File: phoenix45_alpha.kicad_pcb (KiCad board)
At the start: 2 copper layers, 247.7 x 77.5 mm, 125 parts, among them J1 AVR-ISP-6, SW1 SW_PUSH, SW2 SW_PUSH, U1 SRV05-4, U2 ATmega32U4-M, U3 ATmega32U4-M, X1 Crystal_GND24_Small

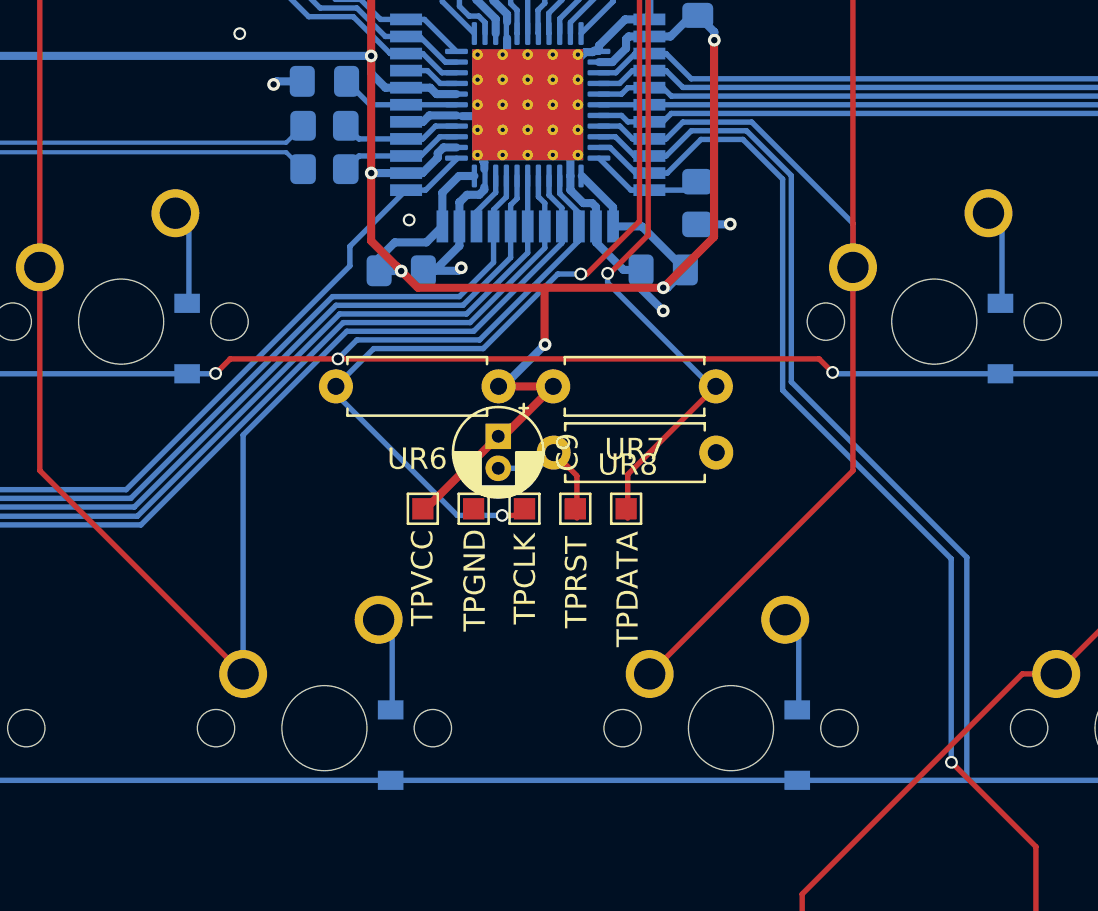
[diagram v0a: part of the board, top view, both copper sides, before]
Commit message: round tracks
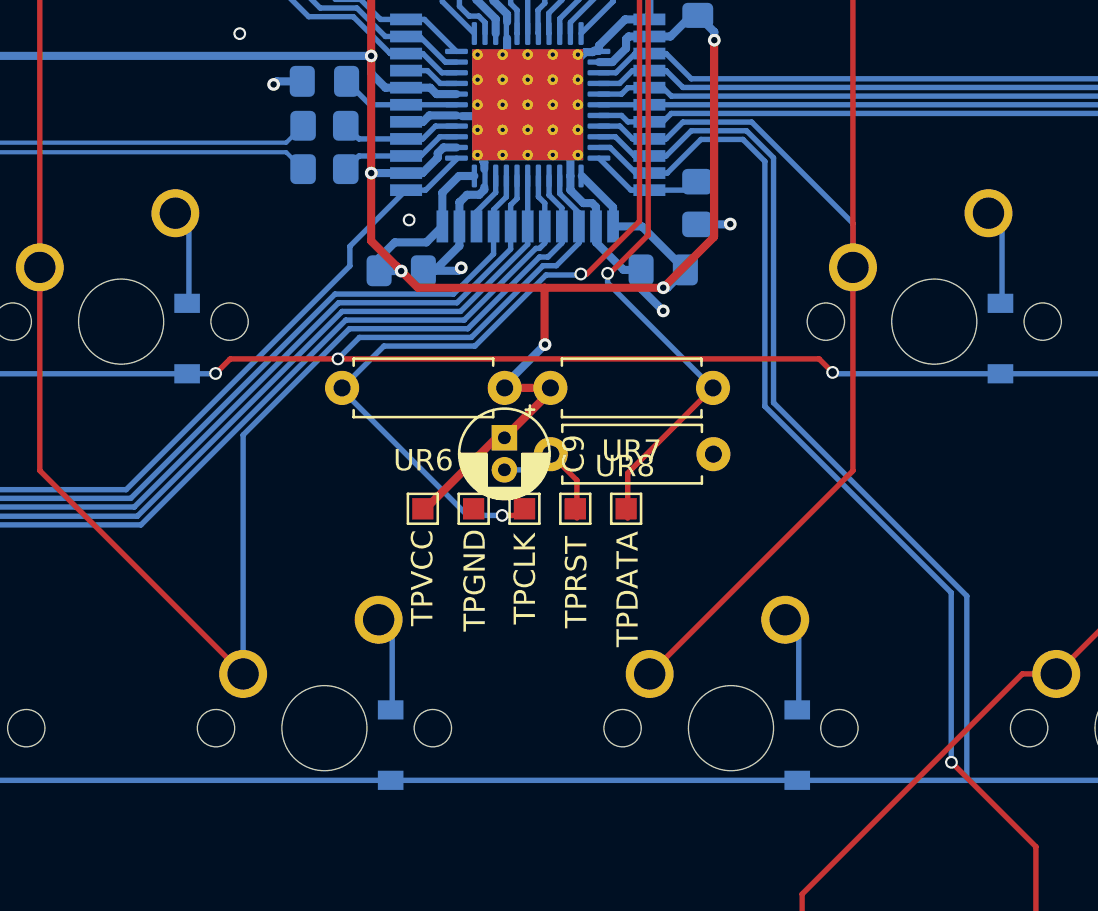
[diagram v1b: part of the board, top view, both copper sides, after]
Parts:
- moved C9 0.30 mm to (148.1, 61.8)
- moved UR6 0.30 mm to (148.1, 59.5)
- moved UR7 0.15 mm to (157.9, 59.5)
- moved UR8 0.15 mm to (150.3, 62.6)
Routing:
- net +5V: track 200.4 -> 199.4 mm

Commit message: MX+choc
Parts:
- removed K_SPACE27, K_SPACE39: KEYSW, MX_Only:MXOnly-1U-NoLED
- K_SPACE1, K_SPACE10, K_SPACE11, K_SPACE12, K_SPACE13, K_SPACE14, K_SPACE15, K_SPACE16, K_SPACE17, K_SPACE18, K_SPACE19, K_SPACE2, K_SPACE21, K_SPACE22, K_SPACE23, K_SPACE24, K_SPACE25, K_SPACE26, K_SPACE28, K_SPACE29, K_SPACE3, K_SPACE30, K_SPACE31, K_SPACE32, K_SPACE34, K_SPACE35, K_SPACE36, K_SPACE37, K_SPACE38, K_SPACE4, K_SPACE41, K_SPACE46, K_SPACE5, K_SPACE6, K_SPACE8, K_SPACE9: footprint MX_Only:MXOnly-1U-NoLED -> kbd:CherryMX_Choc_1u
- K_SPACE20, K_SPACE7: footprint MX_Only:MXOnly-1.5U-NoLED -> kbd:CherryMX_Choc_1.5u
- K_SPACE40, K_SPACE47: footprint MX_Only:MXOnly-1.25U-NoLED -> kbd:CherryMX_Choc_1.5u
- K_SPACE42, K_SPACE45: footprint MX_Only:MXOnly-1.25U-NoLED -> kbd:CherryMX_Choc_1u
- K_SPACE43, K_SPACE44: footprint MX_Only:MXOnly-1.75U-NoLED -> kbd:CherryMX_Choc_1.5u
- moved D_SPACE41 11.1 mm to (95.2, 100.8)
- moved D_SPACE46 11.0 mm to (209.6, 100.8)
- moved K_SPACE41 9.53 mm to (92.1, 94.5)
- moved K_SPACE46 9.53 mm to (206.4, 94.5)
- moved D_SPACE42 9.11 mm to (114.3, 100.8)
- moved D_SPACE45 8.99 mm to (190.5, 100.8)
- moved F1 8.53 mm to (61.0, 44.8)
- moved D_SPACE27 7.89 mm to (42.9, 82.5)
- moved D_SPACE40 7.37 mm to (69.1, 100.8)
- moved D_SPACE47 7.26 mm to (235.7, 100.8)
- moved K_SPACE45 7.14 mm to (187.3, 94.5)
- moved K_SPACE42 7.14 mm to (111.1, 94.5)
- moved D_SPACE14 6.35 mm to (38.1, 63.5)
- moved D_SPACE1 6.35 mm to (38.0, 44.5)
- moved D_SPACE10 6.35 mm to (209.5, 44.5)
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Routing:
- net row2: track 256.8 -> 203.6 mm
- net col2: track 142.6 -> 160.3 mm
- net col3: track 125.1 -> 141.8 mm
- net col4: track 110.8 -> 127.4 mm
- net col1: track 162.1 -> 175.9 mm
- net col10: track 133.8 -> 145.7 mm
- net Net-(D_SPACE4-Pad2): track 3.59 -> 15.3 mm
- net Net-(D_SPACE5-Pad2): track 3.59 -> 15.3 mm
- net Net-(D_SPACE6-Pad2): track 3.59 -> 15.3 mm
- net col0: track 162.4 -> 173.4 mm
- net col9: track 115.2 -> 126.2 mm
- net Net-(D_SPACE14-Pad2): track 3.59 -> 14.2 mm
- net Net-(D_SPACE38-Pad2): track 3.59 -> 14.1 mm
- net Net-(D_SPACE37-Pad2): track 3.59 -> 14.1 mm
- net Net-(D_SPACE36-Pad2): track 3.59 -> 14.1 mm
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
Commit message: go back to MX
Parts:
- added K_SPACE27: KEYSW, MX_Only:MXOnly-1U-NoLED, F.Cu at (44.5, 75.4)
- added K_SPACE39: KEYSW, MX_Only:MXOnly-1U-NoLED, F.Cu at (254.0, 75.4)
- K_SPACE1, K_SPACE10, K_SPACE11, K_SPACE12, K_SPACE13, K_SPACE14, K_SPACE15, K_SPACE16, K_SPACE17, K_SPACE18, K_SPACE19, K_SPACE2, K_SPACE21, K_SPACE22, K_SPACE23, K_SPACE24, K_SPACE25, K_SPACE26, K_SPACE28, K_SPACE29, K_SPACE3, K_SPACE30, K_SPACE31, K_SPACE32, K_SPACE34, K_SPACE35, K_SPACE36, K_SPACE37, K_SPACE38, K_SPACE4, K_SPACE41, K_SPACE46, K_SPACE5, K_SPACE6, K_SPACE8, K_SPACE9: footprint kbd:CherryMX_Choc_1u -> MX_Only:MXOnly-1U-NoLED
- K_SPACE20, K_SPACE7: footprint kbd:CherryMX_Choc_1.5u -> MX_Only:MXOnly-1.5U-NoLED
- K_SPACE40, K_SPACE47: footprint kbd:CherryMX_Choc_1.5u -> MX_Only:MXOnly-1.25U-NoLED
- K_SPACE42, K_SPACE45: footprint kbd:CherryMX_Choc_1u -> MX_Only:MXOnly-1.25U-NoLED
- K_SPACE43, K_SPACE44: footprint kbd:CherryMX_Choc_1.5u -> MX_Only:MXOnly-1.75U-NoLED
- moved D_SPACE41 11.1 mm to (85.7, 95.2)
- moved D_SPACE46 11.0 mm to (219.0, 95.2)
- moved K_SPACE41 9.53 mm to (82.5, 94.5)
- moved K_SPACE46 9.53 mm to (215.9, 94.5)
- moved D_SPACE42 9.11 mm to (107.1, 95.2)
- moved D_SPACE45 8.99 mm to (197.6, 95.2)
- moved F1 8.53 mm to (52.6, 43.9)
- moved D_SPACE27 7.89 mm to (47.5, 76.2)
- moved D_SPACE40 7.37 mm to (64.2, 95.2)
- moved D_SPACE47 7.26 mm to (240.4, 95.2)
- moved K_SPACE45 7.14 mm to (194.5, 94.5)
- moved K_SPACE42 7.14 mm to (104.0, 94.5)
- moved D_SPACE14 6.35 mm to (38.0, 57.1)
- moved D_SPACE1 6.35 mm to (38.0, 38.1)
- moved D_SPACE10 6.35 mm to (209.5, 38.1)
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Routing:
- net row2: track 203.6 -> 256.8 mm
- net col2: track 160.3 -> 142.6 mm
- net col3: track 141.8 -> 125.1 mm
- net col4: track 127.4 -> 110.8 mm
- net col1: track 175.9 -> 162.1 mm
- net col10: track 145.7 -> 133.8 mm
- net Net-(D_SPACE4-Pad2): track 15.3 -> 3.59 mm
- net Net-(D_SPACE5-Pad2): track 15.3 -> 3.59 mm
- net Net-(D_SPACE6-Pad2): track 15.3 -> 3.59 mm
- net col0: track 173.4 -> 162.4 mm
- net col9: track 126.2 -> 115.2 mm
- net Net-(D_SPACE14-Pad2): track 14.2 -> 3.59 mm
- net Net-(D_SPACE38-Pad2): track 14.1 -> 3.59 mm
- net Net-(D_SPACE37-Pad2): track 14.1 -> 3.59 mm
- net Net-(D_SPACE36-Pad2): track 14.1 -> 3.59 mm
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
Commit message: improve trackpoint compatibility; multiple bottom rows, final touch up
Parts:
- added K_SPACE33: KEYSW, MX_Only:MXOnly-1.25U-NoLED, F.Cu at (42.1, 75.4)
- added K_SPACE48: KEYSW, MX_Only:MXOnly-1.25U-NoLED, F.Cu at (256.4, 75.4)
- added K_SPACE49: KEYSW, MX_Only:MXOnly-1.75U-NoLED, F.Cu at (65.9, 94.5)
- added K_SPACE50: KEYSW, MX_Only:MXOnly-1U-NoLED, F.Cu at (92.1, 94.5)
- added K_SPACE51: KEYSW, MX_Only:MXOnly-1U-NoLED, F.Cu at (111.1, 94.5)
- added K_SPACE52: KEYSW, MX_Only:MXOnly-1.5U-NoLED, F.Cu at (134.9, 94.5)
- added K_SPACE53: KEYSW, MX_Only:MXOnly-1.5U-NoLED, F.Cu at (163.5, 94.5)
- added K_SPACE54: KEYSW, MX_Only:MXOnly-1U-NoLED, F.Cu at (187.3, 94.5)
- added K_SPACE55: KEYSW, MX_Only:MXOnly-1U-NoLED, F.Cu at (206.4, 94.5)
- added K_SPACE56: KEYSW, MX_Only:MXOnly-1.75U-NoLED, F.Cu at (232.6, 94.5)
- added K_SPACE57: KEYSW, MX_Only:MXOnly-1.25U-NoLED, F.Cu at (84.9, 94.5)
- added K_SPACE58: KEYSW, MX_Only:MXOnly-1U-NoLED, F.Cu at (106.4, 94.5)
- added K_SPACE59: KEYSW, MX_Only:MXOnly-1U-NoLED, F.Cu at (192.1, 94.5)
- added K_SPACE60: KEYSW, MX_Only:MXOnly-1.25U-NoLED, F.Cu at (213.5, 94.5)
- added SW3: RotaryEncoder_Switch, encoder:RotaryEncoder_Alps_EC11E-Switch_Vertical_H20mm, F.Cu at (156.2, 82.9)
- C9: footprint Capacitor_THT:CP_Radial_D4.0mm_P1.50mm -> Capacitor_SMD:C_0805_2012Metric_Pad1.18x1.45mm_HandSolder; moved to B.Cu
- TP1, TP2, TP3, TP4, TP5: footprint TestPoint:TestPoint_Pad_1.0x1.0mm -> TestPoint:TestPoint_THTPad_1.0x1.0mm_Drill0.5mm
- UR6, UR7, UR8: footprint Resistor_THT:R_Axial_DIN0207_L6.3mm_D2.5mm_P7.62mm_Horizontal -> Resistor_SMD:R_0805_2012Metric_Pad1.20x1.40mm_HandSolder; moved to B.Cu
- moved D_SPACE45 17.4 mm to (180.2, 95.2)
- moved D_SPACE41 9.52 mm to (95.2, 95.2)
- moved D_SPACE42 7.14 mm to (114.2, 95.2)
- moved D_SPACE43 6.43 mm to (142.1, 95.2)
- moved UR7 5.72 mm to (153.2, 62.7), turned to -90 degrees
- moved TP1 5.60 mm to (149.2, 59.5)
- moved TP2 5.60 mm to (144.5, 59.5)
- moved TP3 5.60 mm to (146.8, 59.5)
- moved TP4 5.60 mm to (154.0, 59.5)
- moved TP5 5.60 mm to (151.6, 59.5)
- moved D_SPACE40 4.76 mm to (69.0, 95.2)
- moved UR6 4.21 mm to (145.5, 62.7), turned to 90 degrees
- moved D_SPACE39 4.06 mm to (265.9, 76.2)
- moved D_SPACE46 4.05 mm to (223.0, 95.2)
- moved D_SPACE27 4.05 mm to (51.6, 76.2)
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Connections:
- U2 pad 12: Net-(U2-Pad12) -> row0
- U2 pad 21: row0 -> col12
- U2 pad 25: col12 -> col11
- U2 pad 26: col11 -> col10
- U2 pad 27: col10 -> col9
- U2 pad 28: col9 -> col8
- U2 pad 29: col8 -> col7
- U2 pad 30: col7 -> row2
- U2 pad 31: row2 -> row3
- U2 pad 32: row3 -> encB
- U2 pad 36: row1 -> encA
- U2 pad 37: col5 -> row1
- U2 pad 8: Net-(U2-Pad8) -> col5
- U3 pad 12: Net-(U2-Pad12) -> row0
- U3 pad 21: row0 -> col12
- U3 pad 25: col12 -> col11
- U3 pad 26: col11 -> col10
- U3 pad 27: col10 -> col9
- U3 pad 28: col9 -> col8
- U3 pad 29: col8 -> col7
- U3 pad 30: col7 -> row2
- U3 pad 31: row2 -> row3
- U3 pad 32: row3 -> encB
- U3 pad 36: row1 -> encA
- U3 pad 37: col5 -> row1
- U3 pad 8: Net-(U2-Pad8) -> col5
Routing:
- net encB: track 0.00 -> 51.7 mm, vias 0 -> 1
- net encA: track 0.00 -> 38.5 mm, vias 0 -> 1
- net Net-(D_SPACE45-Pad2): track 3.59 -> 19.9 mm
- net Net-(D_SPACE46-Pad2): track 3.59 -> 17.2 mm
- net PD5: track 43.2 -> 29.8 mm, vias 3 -> 2
- net col5: track 75.3 -> 62.8 mm, vias 0 -> 1
- net col10: track 133.8 -> 143.7 mm
- net col2: track 142.6 -> 152.4 mm
- net Net-(D_SPACE41-Pad2): track 3.59 -> 13.4 mm
- net GND: track 96.1 -> 87.6 mm, vias 18 -> 16
- net col9: track 115.2 -> 122.8 mm
- net col3: track 125.1 -> 132.5 mm
- net Net-(D_SPACE42-Pad2): track 3.59 -> 11.1 mm
- net +5V: track 199.4 -> 206.8 mm
- net col12: track 159.4 -> 166.5 mm
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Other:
- board text added: "1"
- board text added: "1.25u"
- board text added: "1.5u"
- board text added: "1u"
- board text added: "2"
- board text added: "3"

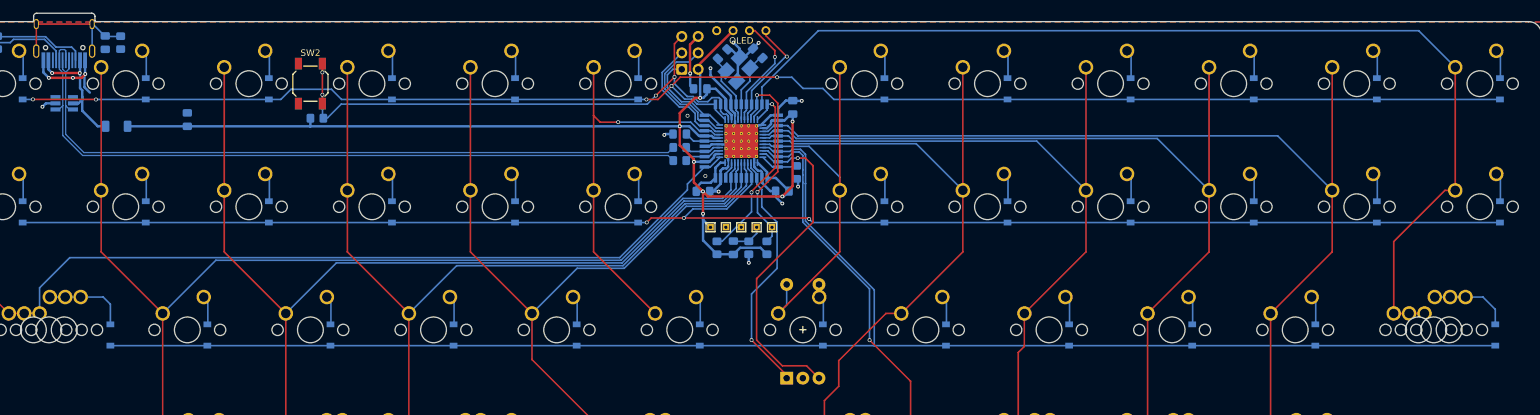
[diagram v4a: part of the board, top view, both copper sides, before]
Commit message: atmega32u4-MU only
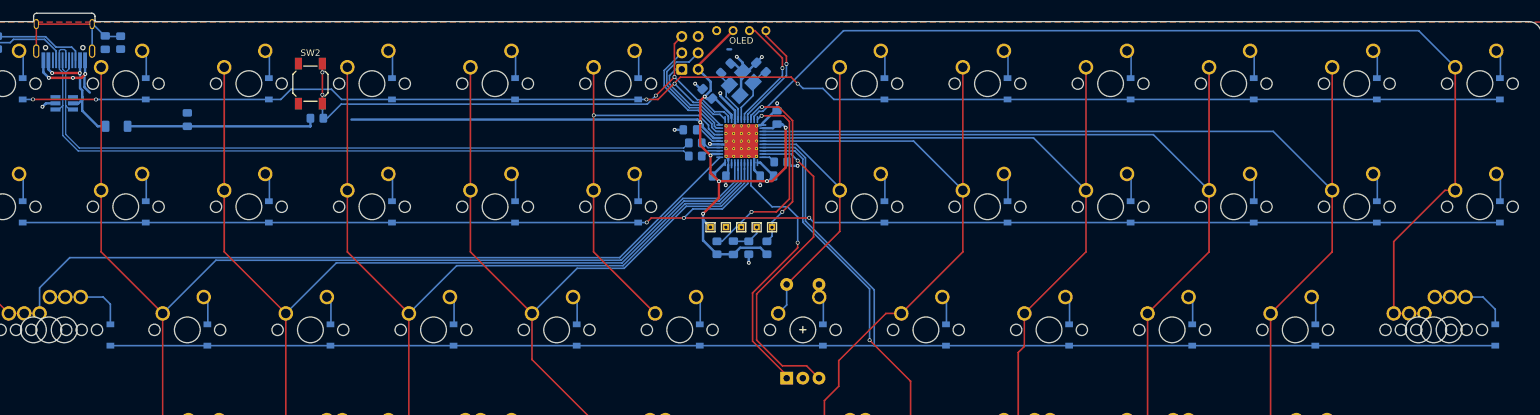
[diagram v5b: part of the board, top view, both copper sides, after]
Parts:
- removed U3: ATmega32U4-M, Package_QFP:TQFP-44_10x10mm_P0.8mm
- moved C2 3.46 mm to (145.8, 51.6)
- moved C3 3.34 mm to (153.2, 51.6)
- moved R2 2.94 mm to (155.3, 49.4), turned to 180 degrees
- moved C4 2.88 mm to (154.8, 42.5)
- moved UR2 2.51 mm to (142.1, 46.5)
- moved UR1 2.51 mm to (142.1, 48.5)
- moved C7 2.25 mm to (152.3, 34.8)
- moved C8 2.25 mm to (146.8, 34.9)
- moved X1 2.25 mm to (149.2, 37.3)
- moved C6 1.72 mm to (141.3, 44.5)
- moved C5 1.35 mm to (144.0, 38.9), turned to 135 degrees
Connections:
- U2 pad 42: Net-(U2-Pad42) -> unconnected-(U2-Pad42)
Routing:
- net +5V: track 206.8 -> 176.3 mm
- net GND: track 87.6 -> 63.6 mm, vias 16 -> 15
- net col7: track 63.1 -> 57.1 mm
- net encA: track 38.5 -> 42.4 mm
- net Net-(R2-Pad2): track 5.68 -> 2.06 mm
- net Net-(U2-Pad4): track 5.69 -> 2.65 mm
- net Net-(U2-Pad3): track 5.82 -> 2.86 mm
- net Net-(C7-Pad1): track 10.7 -> 7.93 mm
- net Net-(U2-Pad42): track 2.74 -> 0.00 mm
- net Net-(C8-Pad1): track 10.7 -> 8.12 mm
- net PD2: track 31.7 -> 29.5 mm
- net RST: track 88.1 -> 85.9 mm
- net PD5: track 29.8 -> 31.9 mm
- net D-: track 112.9 -> 115.0 mm
- net D+: track 110.1 -> 112.2 mm
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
